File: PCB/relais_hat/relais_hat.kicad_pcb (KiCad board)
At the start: 2 copper layers, 85 x 56 mm, 57 parts, among them J1 Conn_01x03, J10 Conn_01x02, J11 Conn_01x02, J12 Conn_01x03, J13 DB9_Female, J14 Conn_01x02, J2 Conn_01x03, J3 Conn_02x04_Odd_Even, J4 Screw_Terminal_01x02, J5 Screw_Terminal_01x02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

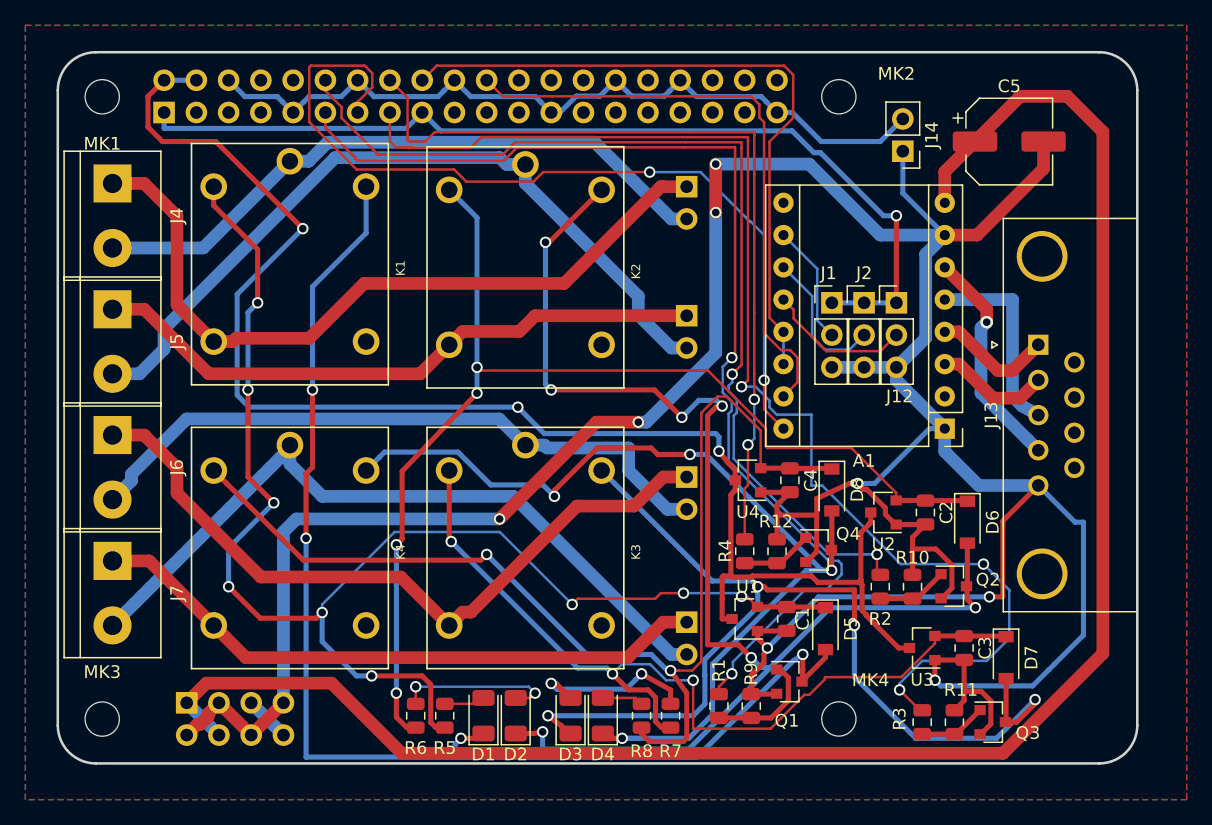
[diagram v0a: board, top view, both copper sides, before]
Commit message: update alim and relais pcb 2-> 4 couches
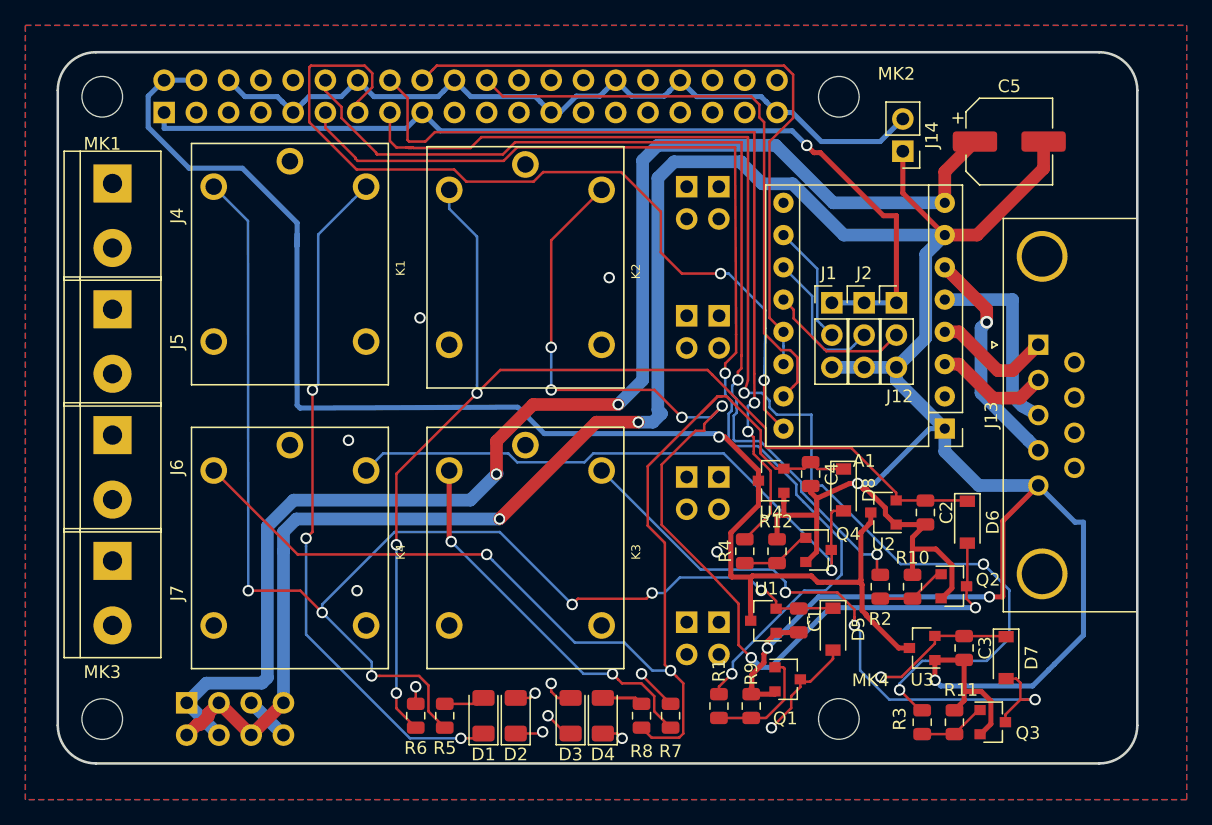
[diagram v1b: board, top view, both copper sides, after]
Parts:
- added J15: Conn_01x02, Connector_PinHeader_2.54mm:PinHeader_1x02_P2.54mm_Vertical, B.Cu at (252.1, 104.3)
- added J16: Conn_01x02, Connector_PinHeader_2.54mm:PinHeader_1x02_P2.54mm_Vertical, B.Cu at (252.1, 127.1)
- added J17: Conn_01x02, Connector_PinHeader_2.54mm:PinHeader_1x02_P2.54mm_Vertical, B.Cu at (252.1, 114.4)
- added J18: Conn_01x02, Connector_PinHeader_2.54mm:PinHeader_1x02_P2.54mm_Vertical, B.Cu at (252.1, 138.6)
- moved U4 1.82 mm to (256.2, 127.4)
- moved C4 1.70 mm to (259.3, 126.9)
- moved U1 1.48 mm to (255.6, 138.5)
- moved C1 0.95 mm to (258.4, 138.4)
- moved D8 0.92 mm to (261.9, 128.2)
- moved D5 0.60 mm to (261.1, 139.1)
- moved Q1 0.22 mm to (257.5, 143.1)
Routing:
- net +12V: track 141.7 -> 108.1 mm, vias 0 -> 2
- net Net-(J11-Pad2): track 61.1 -> 76.3 mm
- net Net-(J15-Pad2): track 51.2 -> 66.0 mm
- net +5V: track 128.1 -> 114.6 mm, vias 3 -> 1
- net Net-(D1-Pad1): track 98.1 -> 89.1 mm
- net Net-(J10-Pad1): track 49.5 -> 57.8 mm
- net Net-(D4-Pad1): track 83.4 -> 75.3 mm, vias 4 -> 2
- net Net-(C3-Pad1): track 69.2 -> 64.5 mm
- net Net-(C1-Pad1): track 106.6 -> 102.7 mm, vias 9 -> 6
- net Net-(D3-Pad1): track 80.8 -> 77.7 mm
- net Net-(C4-Pad1): track 90.2 -> 93.1 mm
- net Net-(J16-Pad1): track 57.4 -> 60.1 mm
- net Net-(D4-Pad2): track 3.49 -> 6.08 mm
- net Net-(J11-Pad1): track 49.2 -> 51.6 mm
- net Net-(J10-Pad2): track 58.9 -> 60.9 mm
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- added copper zone on B.Cu, net GND
- added copper zone on F.Cu, net GND
- added copper zone on In1.Cu, net GND
- added copper zone on In2.Cu, net GND
- removed copper zone on B.Cu, net (none)
- removed copper zone on F.Cu, net (none)
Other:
- copper layers 2 -> 4

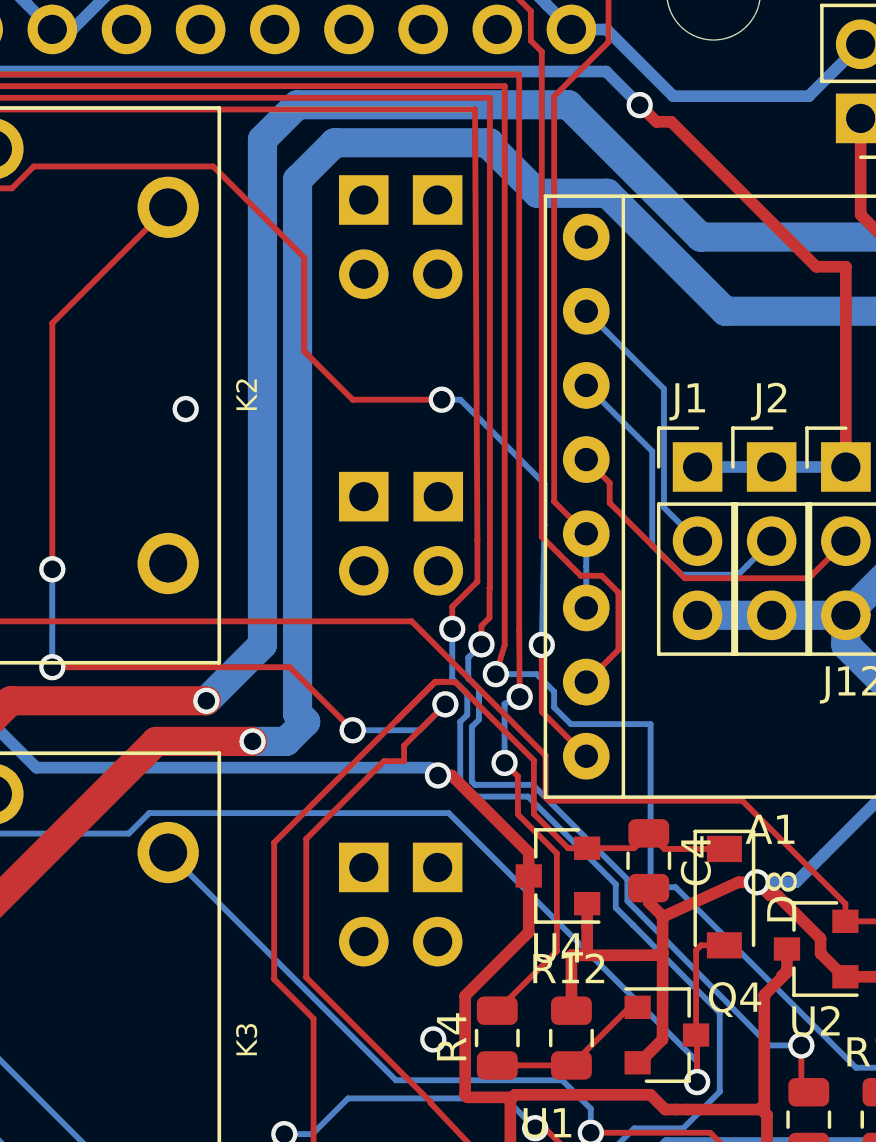
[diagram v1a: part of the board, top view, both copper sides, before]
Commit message: update 3d model and fab file for all board
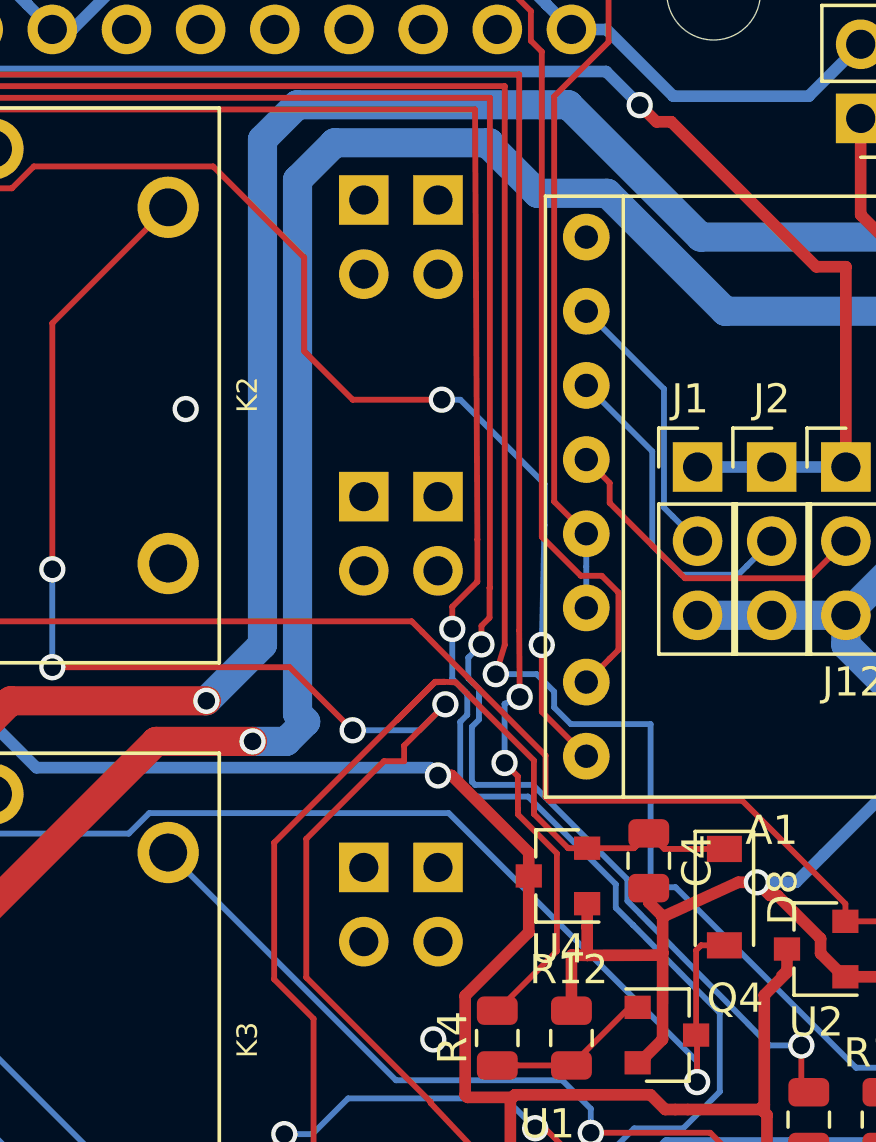
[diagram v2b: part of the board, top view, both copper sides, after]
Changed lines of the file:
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@@
   )
   (layers
-    (0 F.Cu signal)
-    (1 In1.Cu power)
+    (0 F.Cu signal hide)
+    (1 In1.Cu power hide)
     (2 In2.Cu power)
     (31 B.Cu signal)
@@
   )
   (module Connector_PinHeader_2.54mm:PinHeader_1x02_P2.54mm_Vertical (layer B.Cu)
-    (at 252.08 114.44 180)
+    (at 252.07 114.44 180)
     (descr "Through hole straight pin header, 1x02, 2.54mm pitch, single row")
     (tags "Through hole pin header THT 1x02 2.54mm single row")
@@
   )
   (module Connector_PinHeader_2.54mm:PinHeader_1x02_P2.54mm_Vertical (layer B.Cu)
-    (at 252.06 127.14 180)
+    (at 252.07 127.14 180)
     (descr "Through hole straight pin header, 1x02, 2.54mm pitch, single row")
     (tags "Through hole pin header THT 1x02 2.54mm single row")
@@
   )
   (module Connector_PinHeader_2.54mm:PinHeader_1x02_P2.54mm_Vertical (layer B.Cu)
-    (at 252.06 104.28 180)
+    (at 252.07 104.28 180)
     (descr "Through hole straight pin header, 1x02, 2.54mm pitch, single row")
     (tags "Through hole pin header THT 1x02 2.54mm single row")

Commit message: ajust all board
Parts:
- D1, D2, D3, D4: footprint LED_SMD:LED_1206_3216Metric -> LED_SMD:LED_0805_2012Metric
- MK1, MK2, MK3, MK4: value M2.5 -> M3
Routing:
- net Net-(D4-Pad2): track 6.08 -> 3.05 mm
- net Net-(D2-Pad1): track 105.7 -> 106.5 mm
- net +12V: vias 2 -> 4
- net GND: vias 11 -> 10

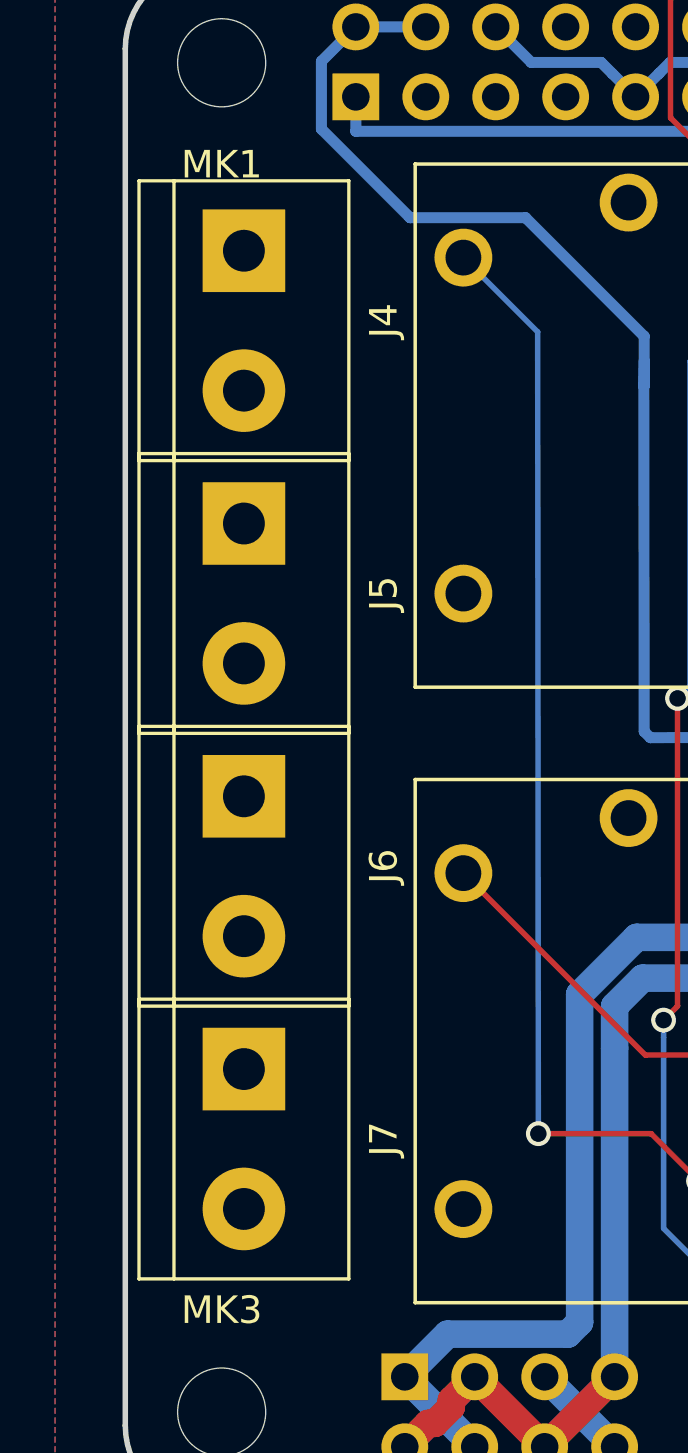
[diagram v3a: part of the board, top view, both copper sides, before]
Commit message: ajust terminal position in relay board
change hole diameter in res_board
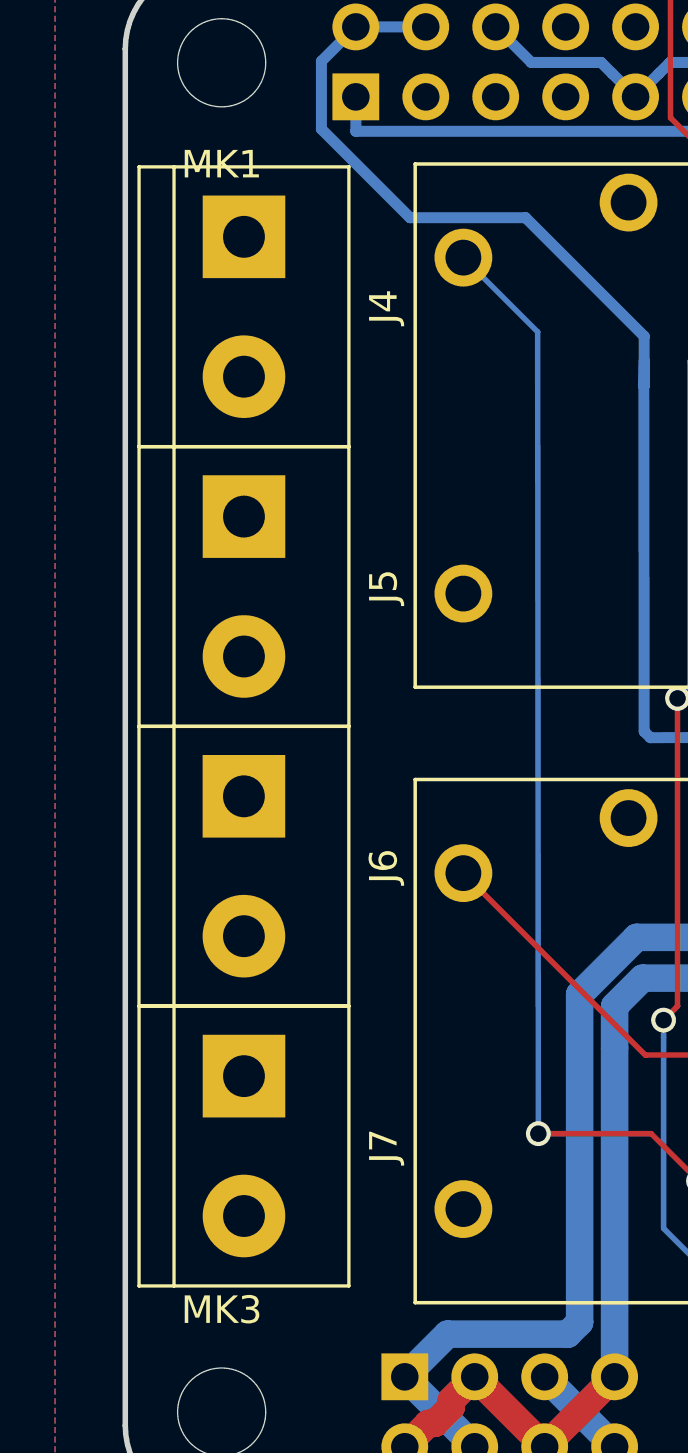
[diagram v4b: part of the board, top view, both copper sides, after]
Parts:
- moved J4 0.51 mm to (204.3, 103.5)
- moved J7 0.26 mm to (204.3, 134.0)
- moved J5 0.25 mm to (204.3, 113.7)
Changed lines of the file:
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@@
   (page A3)
   (title_block
-    (date "15 nov 2012")
+    (date 2020-11-13)
   )
   (layers
@@
   )
   (module TerminalBlock:TerminalBlock_bornier-2_P5.08mm (layer F.Cu)
-    (at 204.318 133.744 270)
+    (at 204.32 134 270)
     (descr "simple 2-pin terminal block, pitch 5.08mm, revamped version of bornier2")
     (tags "terminal block bornier2")
@@
   )
   (module TerminalBlock:TerminalBlock_bornier-2_P5.08mm (layer F.Cu)
-    (at 204.318 113.932 270)
+    (at 204.32 113.68 270)
     (descr "simple 2-pin terminal block, pitch 5.08mm, revamped version of bornier2")
     (tags "terminal block bornier2")
@@
   )
   (module TerminalBlock:TerminalBlock_bornier-2_P5.08mm (layer F.Cu)
-    (at 204.318 104.026 270)
+    (at 204.32 103.52 270)
     (descr "simple 2-pin terminal block, pitch 5.08mm, revamped version of bornier2")
     (tags "terminal block bornier2")
